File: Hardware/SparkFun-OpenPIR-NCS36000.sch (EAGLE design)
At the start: 37 parts, among them J1 3-JST, J2 0.1", U1 NCS36000, U2 PIR

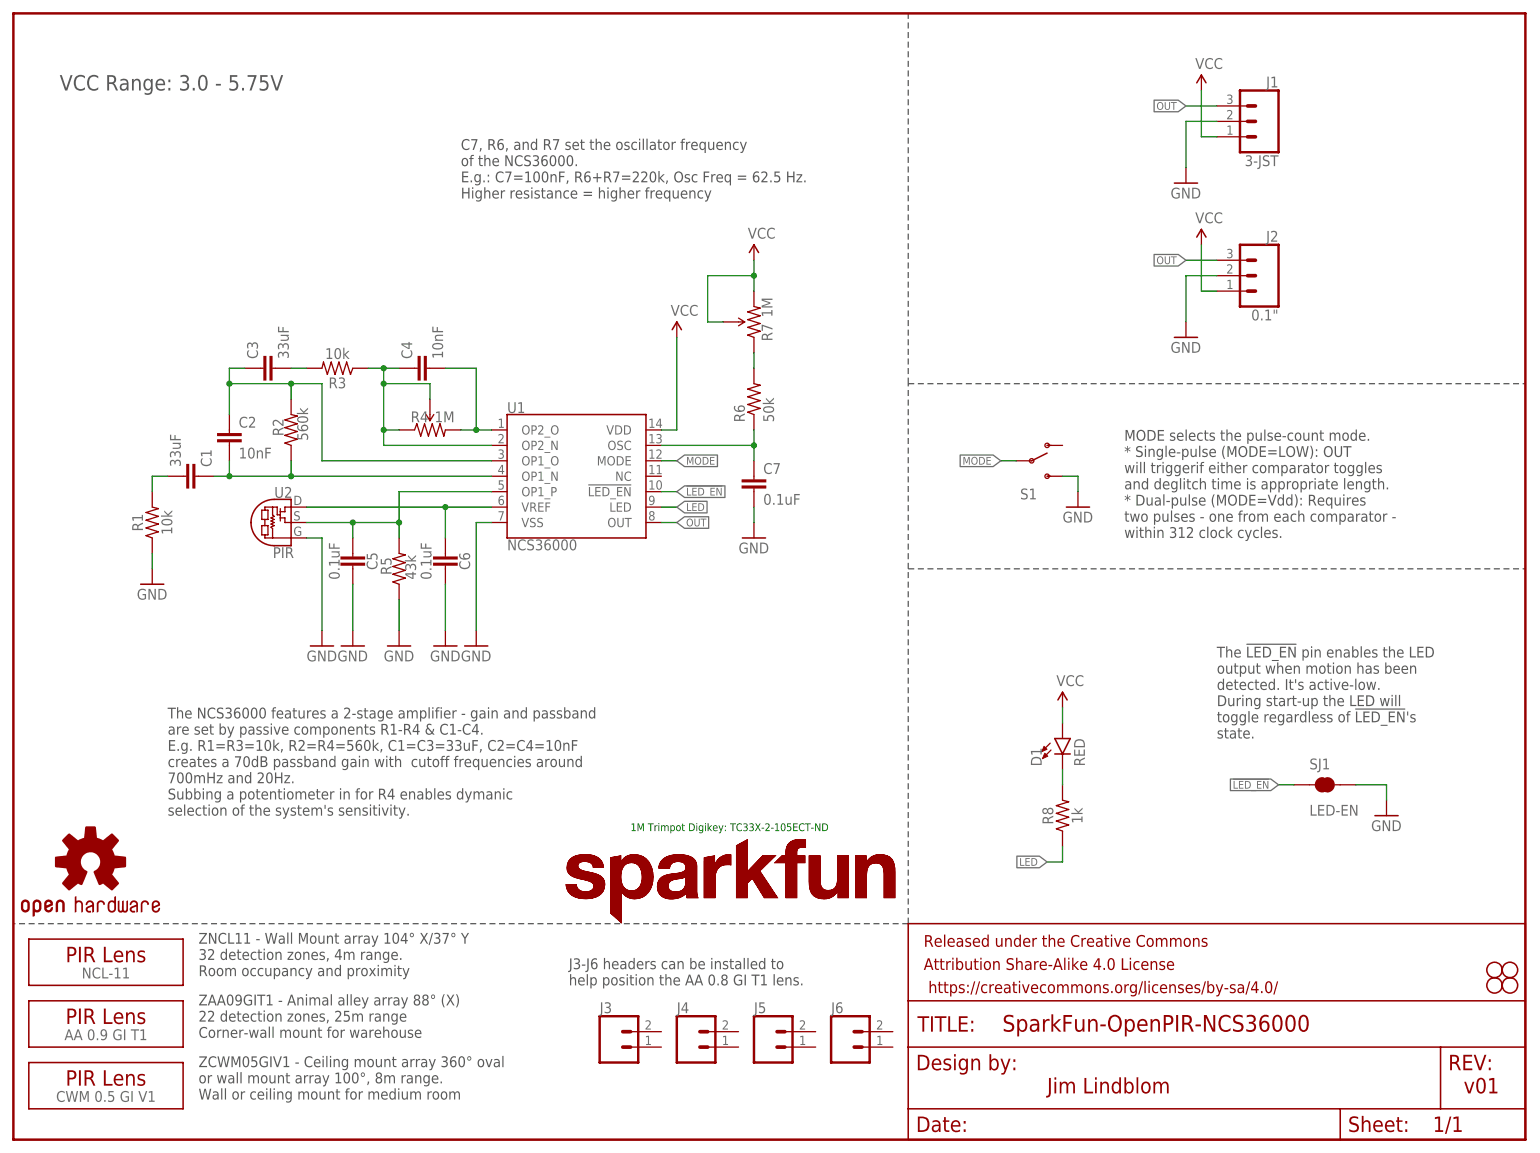
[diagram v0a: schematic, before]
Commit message: Swapping 33uF cap packages to 1206.
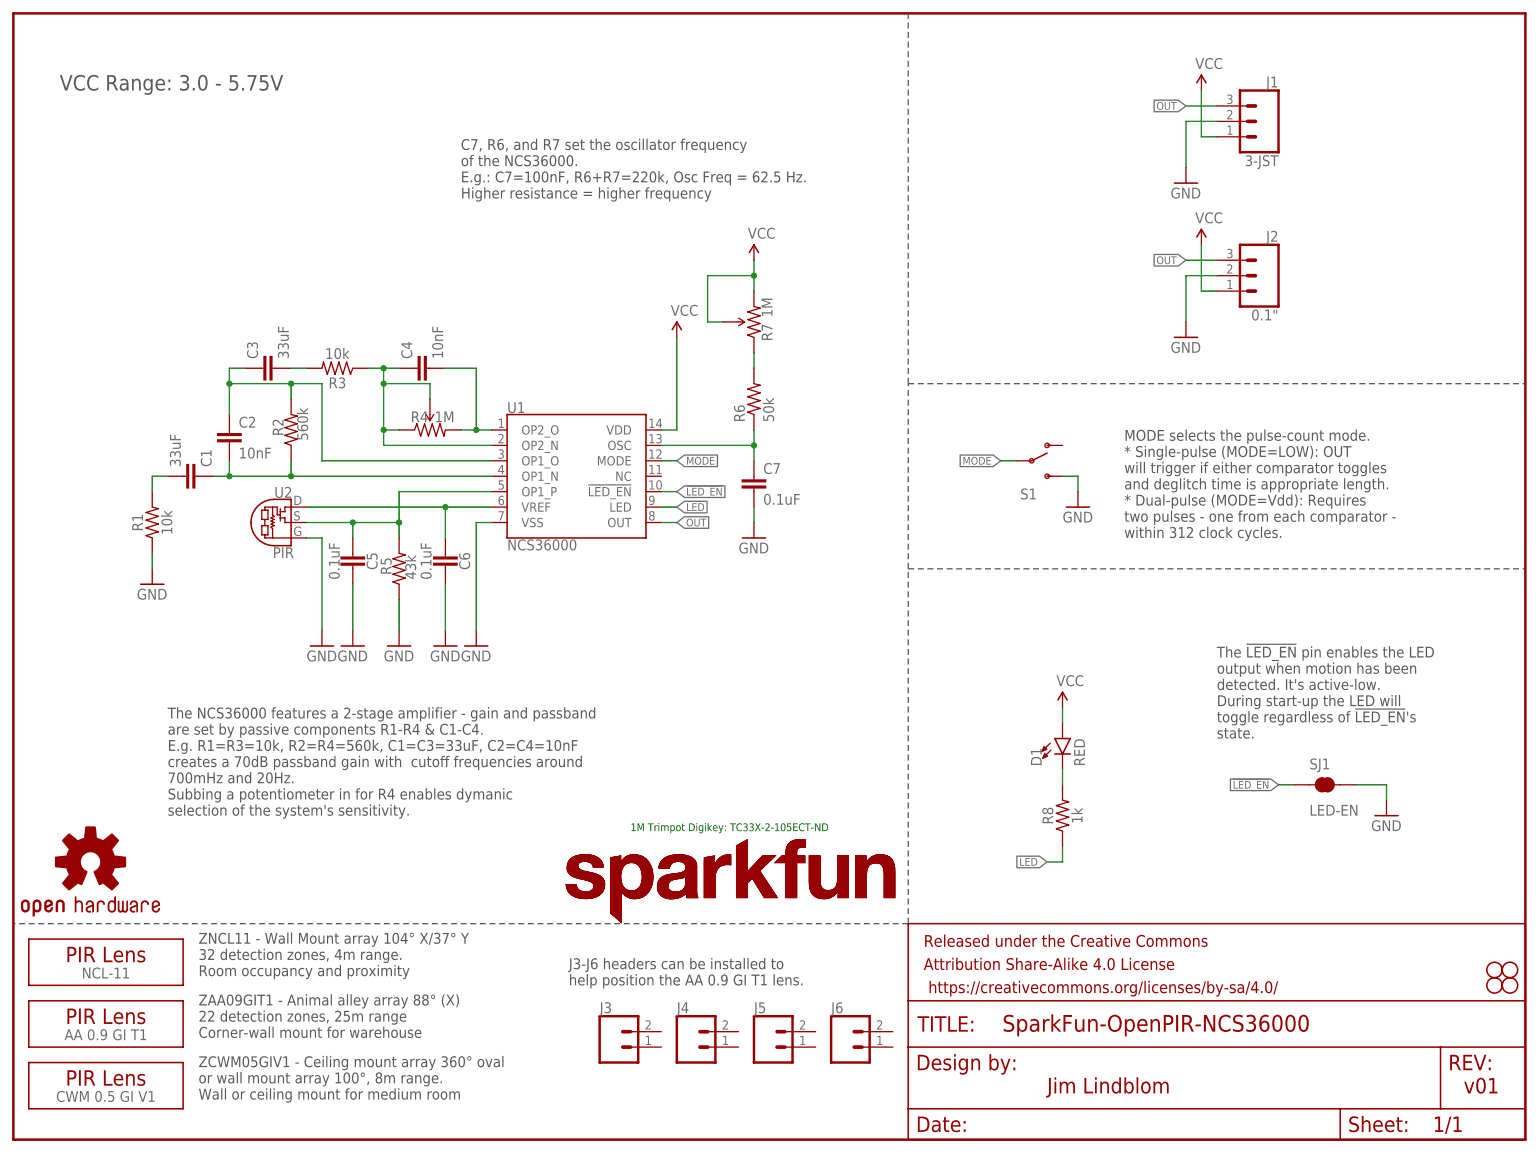
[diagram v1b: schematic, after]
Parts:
- C1, C3: device junkFromCapacitors:CAP0603-CAP -> SparkFun-Passives:CAP1206
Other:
- note added: "J3-J6 headers can be installed to help position the AA 0.9 GI T1 lens."
- note added: "MODE selects the pulse-count mode. * Single-pulse (MODE=LOW): OUT will trigger if either comparator toggles and deglitch time is appropriate length. * Dual-pulse (MODE=Vdd): Requires two pulses - one from each comparator - within 312 clock cycles."
- note removed: "J3-J6 headers can be installed to help position the AA 0.8 GI T1 lens."
- note removed: "MODE selects the pulse-count mode. * Single-pulse (MODE=LOW): OUT will triggerif either comparator toggles and deglitch time is appropriate length. * Dual-pulse (MODE=Vdd): Requires two pulses - one from each comparator - within 312 clock cycles."
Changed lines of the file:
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@@
 <grid distance="0.1" unitdist="inch" unit="inch" style="lines" multiple="1" display="no" altdistance="0.01" altunitdist="inch" altunit="inch"/>
 <layers>
-<layer number="1" name="Top" color="4" fill="1" visible="yes" active="no"/>
-<layer number="2" name="Route2" color="1" fill="3" visible="yes" active="no"/>
-<layer number="3" name="Route3" color="4" fill="3" visible="yes" active="no"/>
-<layer number="4" name="Route4" color="1" fill="4" visible="yes" active="no"/>
-<layer number="5" name="Route5" color="4" fill="4" visible="yes" active="no"/>
-<layer number="6" name="Route6" color="1" fill="8" visible="yes" active="no"/>
-<layer number="7" name="Route7" color="4" fill="8" visible="yes" active="no"/>
-<layer number="8" name="Route8" color="1" fill="2" visible="yes" active="no"/>
-<layer number="9" name="Route9" color="4" fill="2" visible="yes" active="no"/>
-<layer number="10" name="Route10" color="1" fill="7" visible="yes" active="no"/>
-<layer number="11" name="Route11" color="4" fill="7" visible="yes" active="no"/>
-<layer number="12" name="Route12" color="1" fill="5" visible="yes" active="no"/>
-<layer number="13" name="Route13" color="4" fill="5" visible="yes" active="no"/>
-<layer number="14" name="Route14" color="1" fill="6" visible="yes" active="no"/>
-<layer number="15" name="Route15" color="4" fill="6" visible="yes" active="no"/>
-<layer number="16" name="Bottom" color="1" fill="1" visible="yes" active="no"/>
-<layer number="17" name="Pads" color="2" fill="1" visible="yes" active="no"/>
-<layer number="18" name="Vias" color="2" fill="1" visible="yes" active="no"/>
-<layer number="19" name="Unrouted" color="6" fill="1" visible="yes" active="no"/>
-<layer number="20" name="Dimension" color="15" fill="1" visible="yes" active="no"/>
-<layer number="21" name="tPlace" color="16" fill="1" visible="yes" active="no"/>
-<layer number="22" name="bPlace" color="14" fill="1" visible="yes" active="no"/>
-<layer number="23" name="tOrigins" color="15" fill="1" visible="yes" active="no"/>
-<layer number="24" name="bOrigins" color="15" fill="1" visible="yes" active="no"/>
-<layer number="25" name="tNames" color="7" fill="1" visible="yes" active="no"/>
-<layer number="26" name="bNames" color="7" fill="1" visible="yes" active="no"/>
-<layer number="27" name="tValues" color="7" fill="1" visible="yes" active="no"/>
-<layer number="28" name="bValues" color="7" fill="1" visible="yes" active="no"/>
+<layer number="1" name="Top" color="4" fill="1" visible="no" active="no"/>
+<layer number="2" name="Route2" color="1" fill="3" visible="no" active="no"/>
+<layer number="3" name="Route3" color="4" fill="3" visible="no" active="no"/>
+<layer number="4" name="Route4" color="1" fill="4" visible="no" active="no"/>
+<layer number="5" name="Route5" color="4" fill="4" visible="no" active="no"/>
+<layer number="6" name="Route6" color="1" fill="8" visible="no" active="no"/>
+<layer number="7" name="Route7" color="4" fill="8" visible="no" active="no"/>
+<layer number="8" name="Route8" color="1" fill="2" visible="no" active="no"/>
+<layer number="9" name="Route9" color="4" fill="2" visible="no" active="no"/>
+<layer number="10" name="Route10" color="1" fill="7" visible="no" active="no"/>
+<layer number="11" name="Route11" color="4" fill="7" visible="no" active="no"/>
+<layer number="12" name="Route12" color="1" fill="5" visible="no" active="no"/>
+<layer number="13" name="Route13" color="4" fill="5" visible="no" active="no"/>
+<layer number="14" name="Route14" color="1" fill="6" visible="no" active="no"/>
+<layer number="15" name="Route15" color="4" fill="6" visible="no" active="no"/>
+<layer number="16" name="Bottom" color="1" fill="1" visible="no" active="no"/>
+<layer number="17" name="Pads" color="2" fill="1" visible="no" active="no"/>
+<layer number="18" name="Vias" color="2" fill="1" visible="no" active="no"/>
+<layer number="19" name="Unrouted" color="6" fill="1" visible="no" active="no"/>
+<layer number="20" name="Dimension" color="15" fill="1" visible="no" active="no"/>
+<layer number="21" name="tPlace" color="16" fill="1" visible="no" active="no"/>
+<layer number="22" name="bPlace" color="14" fill="1" visible="no" active="no"/>
+<layer number="23" name="tOrigins" color="15" fill="1" visible="no" active="no"/>
+<layer number="24" name="bOrigins" color="15" fill="1" visible="no" active="no"/>
+<layer number="25" name="tNames" color="7" fill="1" visible="no" active="no"/>
+<layer number="26" name="bNames" color="7" fill="1" visible="no" active="no"/>
+<layer number="27" name="tValues" color="7" fill="1" visible="no" active="no"/>
+<layer number="28" name="bValues" color="7" fill="1" visible="no" active="no"/>
 <layer number="29" name="tStop" color="7" fill="3" visible="no" active="no"/>
 <layer number="30" name="bStop" color="7" fill="6" visible="no" active="no"/>
@@
 <layer number="35" name="tGlue" color="7" fill="4" visible="no" active="no"/>
 <layer number="36" name="bGlue" color="7" fill="5" visible="no" active="no"/>
-<layer number="37" name="tTest" color="7" fill="1" visible="yes" active="no"/>
-<layer number="38" name="bTest" color="7" fill="1" visible="yes" active="no"/>
+<layer number="37" name="tTest" color="7" fill="1" visible="no" active="no"/>
+<layer number="38" name="bTest" color="7" fill="1" visible="no" active="no"/>
 <layer number="39" name="tKeepout" color="4" fill="11" visible="no" active="no"/>
 <layer number="40" name="bKeepout" color="1" fill="11" visible="no" active="no"/>
@@
 <layer number="44" name="Drills" color="7" fill="1" visible="no" active="no"/>
 <layer number="45" name="Holes" color="7" fill="1" visible="no" active="no"/>
-<layer number="46" name="Milling" color="3" fill="1" visible="yes" active="no"/>
-<layer number="47" name="Measures" color="7" fill="1" visible="yes" active="no"/>
-<layer number="48" name="Document" color="7" fill="1" visible="yes" active="no"/>
-<layer number="49" name="Reference" color="7" fill="1" visible="yes" active="no"/>
-<layer number="50" name="dxf" color="7" fill="1" visible="yes" active="no"/>
-<layer number="51" name="tDocu" color="6" fill="1" visible="yes" active="no"/>
-<layer number="52" name="bDocu" color="7" fill="1" visible="yes" active="no"/>
-<layer number="53" name="tGND_GNDA" color="7" fill="9" visible="yes" active="no"/>
-<layer number="54" name="bGND_GNDA" color="1" fill="9" visible="yes" active="no"/>
-<layer number="56" name="wert" color="7" fill="1" visible="yes" active="no"/>
-<layer number="57" name="tCAD" color="7" fill="1" visible="yes" active="no"/>
-<layer number="59" name="tCarbon" color="7" fill="1" visible="yes" active="no"/>
-<layer number="60" name="bCarbon" color="7" fill="1" visible="yes" active="no"/>
+<layer number="46" name="Milling" color="3" fill="1" visible="no" active="no"/>
+<layer number="47" name="Measures" color="7" fill="1" visible="no" active="no"/>
+<layer number="48" name="Document" color="7" fill="1" visible="no" active="no"/>
+<layer number="49" name="Reference" color="7" fill="1" visible="no" active="no"/>
+<layer number="50" name="dxf" color="7" fill="1" visible="no" active="no"/>
+<layer number="51" name="tDocu" color="6" fill="1" visible="no" active="no"/>
+<layer number="52" name="bDocu" color="7" fill="1" visible="no" active="no"/>
+<layer number="53" name="tGND_GNDA" color="7" fill="9" visible="no" active="no"/>
+<layer number="54" name="bGND_GNDA" color="1" fill="9" visible="no" active="no"/>
+<layer number="56" name="wert" color="7" fill="1" visible="no" active="no"/>
+<layer number="57" name="tCAD" color="7" fill="1" visible="no" active="no"/>
+<layer number="59" name="tCarbon" color="7" fill="1" visible="no" active="no"/>
+<layer number="60" name="bCarbon" color="7" fill="1" visible="no" active="no"/>
 <layer number="90" name="Modules" color="5" fill="1" visible="yes" active="yes"/>
 <layer number="91" name="Nets" color="2" fill="1" visible="yes" active="yes"/>
@@
 <part name="GND6" library="SparkFun-Aesthetics" deviceset="GND" device=""/>
 <part name="R1" library="SparkFun-Resistors" deviceset="10KOHM" device="-0603-1/10W-1%" value="10k"/>
-<part name="C1" library="junkFromCapacitors" deviceset="CAP" device="0603-CAP" value="33uF"/>
+<part name="C1" library="SparkFun-Passives" deviceset="CAP" device="1206" value="33uF"/>
 <part name="C2" library="SparkFun-Capacitors" deviceset="10NF" device="-0603-50V-10%" value="10nF"/>
 <part name="R2" library="SparkFun-Passives" deviceset="RESISTOR" device="0603-RES" value="560k"/>
-<part name="C3" library="junkFromCapacitors" deviceset="CAP" device="0603-CAP" value="33uF"/>
+<part name="C3" library="SparkFun-Passives" deviceset="CAP" device="1206" value="33uF"/>
 <part name="R3" library="SparkFun-Resistors" deviceset="10KOHM" device="-0603-1/10W-1%" value="10k"/>
 <part name="C4" library="SparkFun-Capacitors" deviceset="10NF" device="-0603-50V-10%" value="10nF"/>
@@
 <text x="182.88" y="99.06" size="1.778" layer="97">MODE selects the pulse-count mode.
 * Single-pulse (MODE=LOW): OUT
-will triggerif either comparator toggles
+will trigger if either comparator toggles
 and deglitch time is appropriate length.
 * Dual-pulse (MODE=Vdd): Requires
@@
 Higher resistance = higher frequency</text>
 <text x="91.44" y="25.4" size="1.778" layer="97" font="vector">J3-J6 headers can be installed to
-help position the AA 0.8 GI T1 lens.</text>
+help position the AA 0.9 GI T1 lens.</text>
 <text x="30.48" y="30.48" size="1.778" layer="97" font="vector" align="center-left">ZNCL11 - Wall Mount array 104° X/37° Y
 32 detection zones, 4m range.

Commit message: Updating sch and brd after running checklist.
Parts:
- removed J1: 3-JST, openPIR-temp:CONN_03JST-PTH-VERT-NO-SILK
- added FD1, FD2: FIDUCIALUFIDUCIAL, SparkFun-Aesthetics:FIDUCIALUFIDUCIAL
- added J8: (no value), SparkFun-Connectors:CONN_04NO_SILK_ALL_ROUND
- C1, C3: value 33uF -> 22uF; device SparkFun-Passives:CAP1206 -> SparkFun-Capacitors:22UF-0805-6.3V-20%
- D1: value RED -> Green; device SparkFun-LED:LED-RED0603 -> SparkFun-LED:LED-GREEN1206-BOTTOM
- J2: value 0.1" -> (none); device SparkFun-Connectors:CONN_031X03_NO_SILK -> openPIR-temp:CONN_04JST-PTH-VERT-NS
- R2: device SparkFun-Passives:RESISTOR0603-RES -> openPIR-temp:560KOHM-0603-1/10W-5%
- R4, R7: device openPIR-temp:TRIMPOTTX33X -> openPIR-temp:TRIMPOTTX33X-1M
- R5: device SparkFun-Passives:RESISTOR0603-RES -> SparkFun-Resistors:43KOHM-0603-1/10W-1%
- R6: value 50k -> 51k; device SparkFun-Passives:RESISTOR0603-RES -> openPIR-temp:51KOHM-0603-1/10W-1%
- SJ1: device SparkFun-Retired:SOLDERJUMPERNC2 -> SparkFun-Retired:SOLDERJUMPERNC
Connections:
- removed net N$10: C4.2, R4.CW, U1.OP2_O
- new net A_OUT: C4.2, J2.1, J8.1, R4.CW, U1.OP2_O
- net GND: now also J2.3, J8.3; no longer J1.2, J2.2
- net OUT: now also J2.4, J8.4; no longer J1.3, J2.3
- net VCC: now also J2.2, J8.2; no longer J1.1, J2.1
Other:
- note removed: "1M Trimpot Digikey: TC33X-2-105ECT-ND"
